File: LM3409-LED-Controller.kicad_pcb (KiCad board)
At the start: 2 copper layers, 63.5 x 25.4 mm, 48 parts, among them J1 PWM_IN, J2 IADJ, J4 LED+, J5 LED-, J6 EN, Q1 DMPH6050SK3, Q2 ZXMN7A11K, U1 LM3409HV-Q1

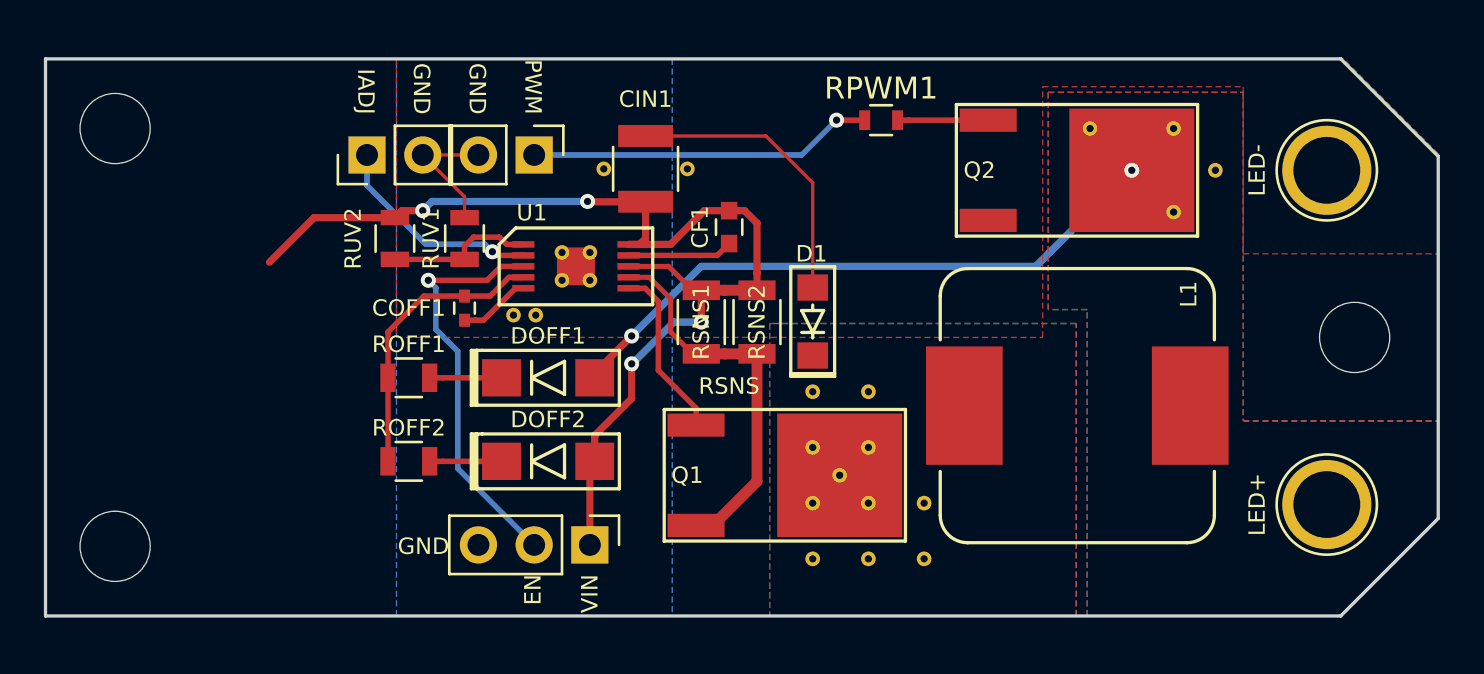
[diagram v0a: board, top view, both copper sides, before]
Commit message: Replace parallel FET with CSD19538Q2 100-V, 49-mΩ NexFET. Added UCC27511 Gate Driver.
Redesign based on TI Designs: TIDA-01415.
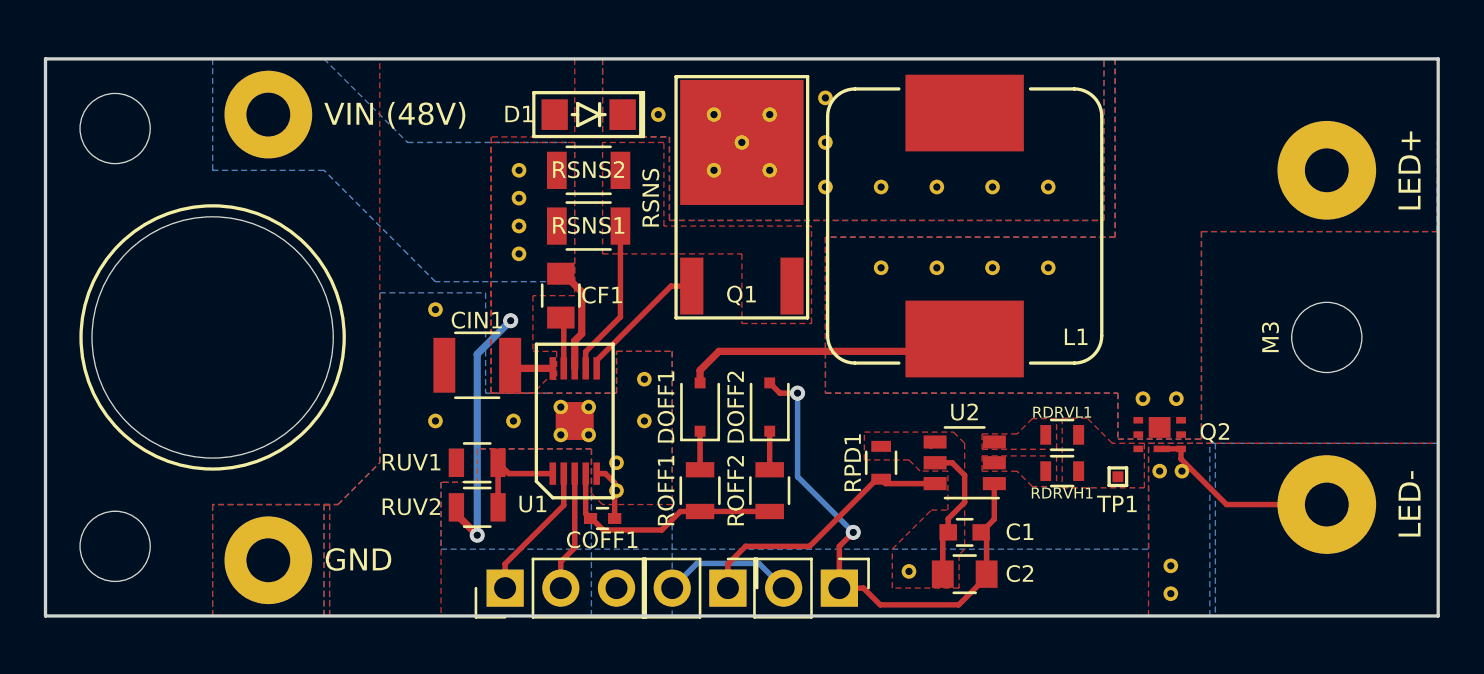
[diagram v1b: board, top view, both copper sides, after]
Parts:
- removed the REF** at (143.5, 116.3)
- removed the REF** at (130.2, 134.0)
- removed the REF** at (125.1, 128.9)
- removed the REF** at (125.1, 131.4)
- removed the REF** at (127.6, 131.4)
- removed the REF** at (127.6, 128.9)
- removed the REF** at (126.3, 130.2)
- removed the REF** at (130.2, 131.4)
- removed the REF** at (127.6, 134.0)
- removed the REF** at (125.1, 134.0)
- removed the REF** at (119.4, 116.2)
- removed the REF** at (141.6, 118.2)
- removed the REF** at (115.6, 116.2)
- removed the REF** at (111.5, 122.9)
- removed the REF** at (113.7, 121.3)
- removed the REF** at (113.7, 120.0)
- removed the REF** at (114.9, 120.0)
- removed the REF** at (114.9, 121.3)
- removed the REF** at (127.6, 126.4)
- removed the REF** at (141.6, 114.4)
- removed the REF** at (137.7, 114.4)
- removed the REF** at (112.5, 122.9)
- removed the REF** at (125.1, 126.4)
- removed RPWM1: 75, Resistors_SMD:R_0603
- added C1: 0.1uF, Capacitors_SMD:C_0603, F.Cu at (132.0, 132.8)
- added C2: 1uF, Capacitors_SMD:C_0805, F.Cu at (132.0, 134.7)
- added J3: PanelMountJack, Project_Footprints:PanelMountJack_11mm, F.Cu at (97.7, 123.9)
- added J7: CONN_1X2, Wire_Connections_Bridges:WireConnection_2.00mmDrill, F.Cu at (100.3, 123.7)
- added RDRVH1: 1.0, Resistors_SMD:R_0603, F.Cu at (136.5, 130.0)
- added RDRVL1: 1.0, Resistors_SMD:R_0603, F.Cu at (136.5, 128.3)
- added REF**: VIA-0.33mm, Project_Footprints:VIA-0.33mm, F.Cu at (125.7, 117.0)
- added REF**: VIA-0.33mm, Project_Footprints:VIA-0.33mm, F.Cu at (118.1, 113.7)
- added REF**: VIA-0.33mm, Project_Footprints:VIA-0.33mm, F.Cu at (116.2, 130.9)
- added REF**: VIA-0.33mm, Project_Footprints:VIA-0.33mm, F.Cu at (141.9, 130.0)
- added REF**: VIA-0.33mm, Project_Footprints:VIA-0.33mm, F.Cu at (140.9, 130.0)
- added REF**: VIA-0.33mm, Project_Footprints:VIA-0.33mm, F.Cu at (111.5, 127.7)
- added REF**: VIA-0.33mm, Project_Footprints:VIA-0.33mm, F.Cu at (129.5, 134.6)
- added REF**: VIA-0.33mm, Project_Footprints:VIA-0.33mm, F.Cu at (111.7, 116.3)
- added REF**: VIA-0.33mm, Project_Footprints:VIA-0.33mm, F.Cu at (111.7, 120.1)
- added REF**: VIA-0.33mm, Project_Footprints:VIA-0.33mm, F.Cu at (117.4, 127.7)
- added REF**: VIA-0.33mm, Project_Footprints:VIA-0.33mm, F.Cu at (117.4, 125.8)
- added REF**: VIA-0.33mm, Project_Footprints:VIA-0.33mm, F.Cu at (135.8, 117.0)
- added REF**: VIA-0.33mm, Project_Footprints:VIA-0.33mm, F.Cu at (140.2, 126.7)
- added REF**: VIA-0.33mm, Project_Footprints:VIA-0.33mm, F.Cu at (141.7, 126.7)
- added REF**: VIA-0.33mm, Project_Footprints:VIA-0.33mm, F.Cu at (128.2, 117.0)
- added REF**: VIA-0.33mm, Project_Footprints:VIA-0.33mm, F.Cu at (125.7, 115.0)
- added REF**: VIA-0.33mm, Project_Footprints:VIA-0.33mm, F.Cu at (120.6, 116.3)
- added REF**: VIA-0.33mm, Project_Footprints:VIA-0.33mm, F.Cu at (123.1, 116.3)
- added REF**: VIA-0.33mm, Project_Footprints:VIA-0.33mm, F.Cu at (123.1, 113.7)
- added REF**: VIA-0.33mm, Project_Footprints:VIA-0.33mm, F.Cu at (120.6, 113.7)
- added REF**: VIA-0.33mm, Project_Footprints:VIA-0.33mm, F.Cu at (121.9, 115.0)
- added REF**: VIA-0.33mm, Project_Footprints:VIA-0.33mm, F.Cu at (141.4, 135.6)
- added REF**: VIA-0.33mm, Project_Footprints:VIA-0.33mm, F.Cu at (133.3, 117.0)
- added REF**: VIA-0.33mm, Project_Footprints:VIA-0.33mm, F.Cu at (141.4, 134.3)
- added REF**: VIA-0.33mm, Project_Footprints:VIA-0.33mm, F.Cu at (113.6, 128.3)
- added REF**: VIA-0.33mm, Project_Footprints:VIA-0.33mm, F.Cu at (114.9, 128.3)
- added REF**: VIA-0.33mm, Project_Footprints:VIA-0.33mm, F.Cu at (114.9, 127.1)
- added REF**: VIA-0.33mm, Project_Footprints:VIA-0.33mm, F.Cu at (113.6, 127.1)
- added REF**: VIA-0.33mm, Project_Footprints:VIA-0.33mm, F.Cu at (116.2, 129.6)
- added REF**: VIA-0.33mm, Project_Footprints:VIA-0.33mm, F.Cu at (107.9, 127.7)
- added REF**: VIA-0.33mm, Project_Footprints:VIA-0.33mm, F.Cu at (107.9, 122.6)
- added REF**: VIA-0.33mm, Project_Footprints:VIA-0.33mm, F.Cu at (111.7, 118.8)
- added REF**: VIA-0.33mm, Project_Footprints:VIA-0.33mm, F.Cu at (130.8, 117.0)
- added REF**: VIA-0.33mm, Project_Footprints:VIA-0.33mm, F.Cu at (111.7, 117.5)
- added REF**: VIA-0.33mm, Project_Footprints:VIA-0.33mm, F.Cu at (128.2, 120.7)
- added REF**: VIA-0.33mm, Project_Footprints:VIA-0.33mm, F.Cu at (135.8, 120.7)
- added REF**: VIA-0.33mm, Project_Footprints:VIA-0.33mm, F.Cu at (133.3, 120.7)
- added REF**: VIA-0.33mm, Project_Footprints:VIA-0.33mm, F.Cu at (130.8, 120.7)
- added REF**: VIA-0.33mm, Project_Footprints:VIA-0.33mm, F.Cu at (125.7, 113.0)
- added RPD1: 10.0k, Resistors_SMD:R_0603, F.Cu at (128.2, 129.6)
- added TP1: TP1, Project_Footprints:Test_Point_1mm, F.Cu at (139.0, 130.2)
- added U2: UCC27511DBVR, Project_Footprints:SOT-23-1.75mm_3.0mm, F.Cu at (132.0, 129.6)
- CF1: footprint Capacitors_SMD:C_0603 -> Capacitors_SMD:C_0805
- DOFF1, DOFF2: value S1ATR -> B0530WS RRG; footprint Project_Footprints:D_2026 -> Diodes_SMD:D_SOD-323F
- J2: value IADJ -> 12V
- J4, J5: footprint Connectors:1pin -> Wire_Pads:SolderWirePad_single_2mmDrill
- Q2: value ZXMN7A11K -> CSD19538Q2T; footprint Project_Footprints:TO252_DPAK -> Project_Footprints:SON_2mm_2mm_thermal
- ROFF2: value 649 -> 23.7k
- moved J2 29.2 mm to (126.3, 135.3), turned to 270 degrees
- moved J1 21.6 mm to (121.2, 135.3)
- moved ROFF2 16.5 mm to (123.1, 130.9), turned to 90 degrees
- moved J4 15.2 mm to (148.5, 116.3)
- moved J5 15.2 mm to (148.5, 131.5)
- moved ROFF1 14.2 mm to (120.0, 130.9), turned to 90 degrees
- moved D1 13.9 mm to (114.9, 113.7), turned to 180 degrees
- moved Q1 12.8 mm to (121.9, 117.5), turned to 90 degrees
- moved RUV2 12.8 mm to (109.8, 131.6), turned to 0 degrees
- moved Q2 12.6 mm to (140.9, 128.3)
- moved CIN1 11.8 mm to (109.8, 125.2), turned to 180 degrees
- moved COFF1 11.5 mm to (115.5, 132.1), turned to 0 degrees
- moved DOFF2 10.4 mm to (123.1, 127.1), turned to 90 degrees
- moved RSNS2 10.3 mm to (114.9, 116.3), turned to 0 degrees
- moved RUV1 10.2 mm to (109.8, 129.6), turned to 180 degrees
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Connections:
- DOFF2 pad 2: VSS -> +12V
- J2 pad 1: IADJ -> +12V
- J6 pad 1: VSS -> IADJ
- Q2 pad 1: Net-(Q2-Pad1) -> D+
- Q2 pad 3: GND -> /FDRV
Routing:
- net VSS: track 52.1 -> 19.0 mm, vias 4 -> 2
- net +12V: track 0.00 -> 23.8 mm, vias 0 -> 2
- net D+: track 28.6 -> 13.4 mm, vias 2 -> 0
- net /EN: track 18.7 -> 5.48 mm, vias 1 -> 0
- net /CSN: track 16.8 -> 7.15 mm
- net Net-(Q2-Pad1): track 4.13 -> 0.00 mm
- net IADJ: track 9.84 -> 6.33 mm, vias 1 -> 0
- net /PWM: track 15.7 -> 12.2 mm, vias 1 -> 0
- net /VCC: track 4.81 -> 2.37 mm
- net /COFF: track 13.2 -> 10.9 mm
- net /PGATE: track 7.96 -> 6.10 mm
- net /UVLO: track 6.76 -> 5.03 mm
- net Net-(DOFF2-Pad1): track 3.28 -> 1.76 mm
- net Net-(DOFF1-Pad1): track 3.28 -> 1.76 mm
- net GND: track 23.1 -> 24.3 mm
- added copper zone on F.Cu, net /CSN
- added copper zone on F.Cu, net /FDRV
- added copper zone on F.Cu, net /OUTH
- added copper zone on F.Cu, net /OUTL
- added copper zone on B.Cu, net VSS
- added copper zone on F.Cu, net VSS
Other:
- outline, holes or cut-outs redrawn
- board text added: "12+"
- board text added: "LED+"
- board text added: "LED-"
- board text added: "M3"
- board text added: "VIN (48V)"
- board text removed: "VIN"

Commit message: Changed secondary voltage input to 9V
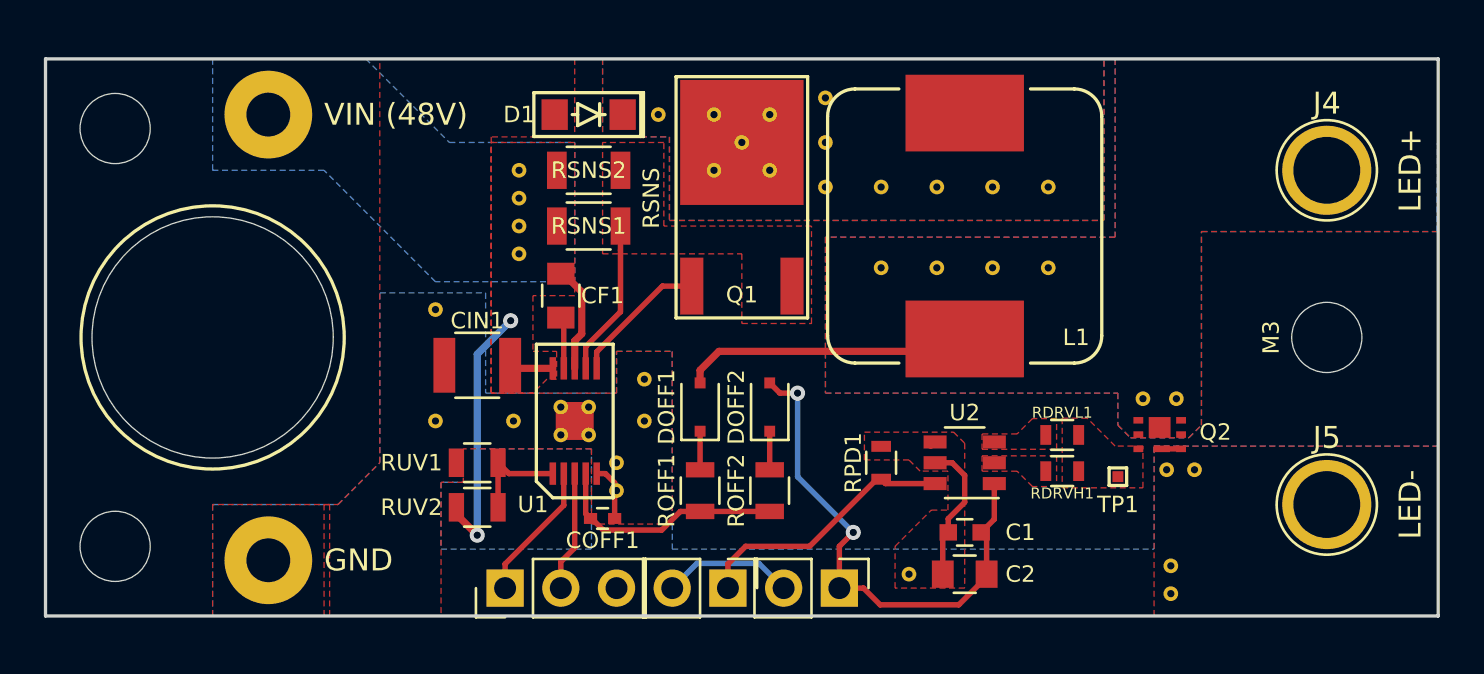
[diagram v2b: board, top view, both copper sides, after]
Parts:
- J2: value 12V -> 9V
- J4, J5: footprint Wire_Pads:SolderWirePad_single_2mmDrill -> Connectors:1pin
- moved REF** 0.58 mm to (142.5, 129.9)
- moved REF** 0.32 mm to (141.2, 129.9)
- moved REF** 0.13 mm to (129.5, 134.7)
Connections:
- net +12V renamed +9V
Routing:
- net GND: track 24.3 -> 16.3 mm
